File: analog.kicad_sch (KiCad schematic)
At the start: 21 parts, among them U10 OPA310xDBV, U11 MCP1501-30xSN, U12 MCP3561R-E/ST, U13 AD5761RBRUZ-RL7

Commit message: Fix Pranav review suggestions
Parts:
- D5: symbol Device:D_Photo -> Sensor_Optical:S5971
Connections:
- net GNDA: now also D5.2 (C), D5.3 (A); no longer D5.1 (K)
- net at C16.2, R6.1, U10.4 (-): now also D5.1 (K); no longer D5.2 (A)
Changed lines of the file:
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@@
+	)
+	(junction
+		(at 44.45 116.84)
+		(diameter 0)
+		(color 0 0 0 0)
 	)
 	(junction
@@
 	(wire
 		(pts
-			(xy 44.45 110.49) (xy 44.45 107.95)
-		)
-		(stroke
-			(width 0)
-			(type default)
-		)
-	)
-	(wire
-		(pts
 			(xy 144.78 118.11) (xy 144.78 116.84)
 		)
@@
 	(wire
 		(pts
+			(xy 36.83 107.95) (xy 36.83 116.84)
+		)
+		(stroke
+			(width 0)
+			(type default)
+		)
+	)
+	(wire
+		(pts
 			(xy 129.54 39.37) (xy 129.54 35.56)
 		)
@@
 	(wire
 		(pts
+			(xy 44.45 115.57) (xy 44.45 116.84)
+		)
+		(stroke
+			(width 0)
+			(type default)
+		)
+	)
+	(wire
+		(pts
 			(xy 227.33 82.55) (xy 233.68 82.55)
 		)
@@
 	(wire
 		(pts
+			(xy 44.45 116.84) (xy 44.45 118.11)
+		)
+		(stroke
+			(width 0)
+			(type default)
+		)
+	)
+	(wire
+		(pts
 			(xy 29.21 95.25) (xy 29.21 91.44)
 		)
@@
 		(pts
 			(xy 86.36 95.25) (xy 86.36 93.98)
+		)
+		(stroke
+			(width 0)
+			(type default)
+		)
+	)
+	(wire
+		(pts
+			(xy 36.83 116.84) (xy 44.45 116.84)
 		)
 		(stroke
@@
 	)
 	(symbol
-		(lib_id "Device:D_Photo")
-		(at 44.45 102.87 90)
+		(lib_id "Sensor_Optical:S5971")
+		(at 44.45 107.95 270)
 		(unit 1)
 		(exclude_from_sim no)
@@
 		(fields_autoplaced yes)
 		(property "Reference" "D5"
-			(at 46.99 102.5524 90)
-			(effects
-				(font
-					(size 1.27 1.27)
-				)
-				(justify right)
+			(at 49.53 106.6799 90)
+			(effects
+				(font
+					(size 1.27 1.27)
+				)
+				(justify left)
 			)
 		)
 		(property "Value" "D_Photo"
-			(at 46.99 105.0924 90)
-			(effects
-				(font
-					(size 1.27 1.27)
-				)
-				(justify right)
+			(at 49.53 109.2199 90)
+			(effects
+				(font
+					(size 1.27 1.27)
+				)
+				(justify left)
 			)
 		)
 		(property "Footprint" "Package_TO_SOT_THT:TO-5-3"
-			(at 44.45 104.14 0)
-			(effects
-				(font
-					(size 1.27 1.27)
-				)
-				(hide yes)
-			)
-		)
-		(property "Datasheet" "~"
-			(at 44.45 104.14 0)
-			(effects
-				(font
-					(size 1.27 1.27)
-				)
-				(hide yes)
-			)
-		)
-		(property "Description" "Photodiode"
-			(at 44.45 102.87 0)
+			(at 53.34 107.95 0)
+			(effects
+				(font
+					(size 1.27 1.27)
+				)
+				(hide yes)
+			)
+		)
+		(property "Datasheet" "https://www.hamamatsu.com/resources/pdf/ssd/s5971_etc_kpin1025e.pdf"
+			(at 44.45 107.95 0)
+			(effects
+				(font
+					(size 1.27 1.27)
+				)
+				(hide yes)
+			)
+		)
+		(property "Description" "Si PIN Photodiode, 0.1 GHz, TO-18-3"
+			(at 44.45 107.95 0)
 			(effects
 				(font
@@
 		)
 		(pin "1"
+		)
+		(pin "3"
 		)
 		(instances
@@
 	(symbol
 		(lib_id "power:GNDA")
-		(at 44.45 110.49 0)
+		(at 44.45 118.11 0)
 		(unit 1)
 		(exclude_from_sim no)
@@
 		(fields_autoplaced yes)
 		(property "Reference" "#PWR041"
-			(at 44.45 116.84 0)
+			(at 44.45 124.46 0)
 			(effects
 				(font
@@
 		)
 		(property "Value" "GNDA"
-			(at 44.45 115.57 0)
+			(at 44.45 123.19 0)
 			(effects
 				(font
@@
 		)
 		(property "Footprint" ""
-			(at 44.45 110.49 0)
+			(at 44.45 118.11 0)
 			(effects
 				(font
@@
 		)
 		(property "Datasheet" ""
-			(at 44.45 110.49 0)
+			(at 44.45 118.11 0)
 			(effects
 				(font
@@
 		)
 		(property "Description" "Power symbol creates a global label with name \"GNDA\" , analog ground"
-			(at 44.45 110.49 0)
-			(effects
-				(font
+			(at 44.45 118.11 0)
+			(effects
+				(font

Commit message: Fix review suggestions from non-fpga board
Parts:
- added C44: 10uF, Capacitor_SMD:C_0805_2012Metric_Pad1.18x1.45mm_HandSolder, symbol Device:C
- added R15: 10kR, Resistor_SMD:R_0805_2012Metric_Pad1.20x1.40mm_HandSolder, symbol Device:R_US
- added U16: OPA310xDBV, Package_TO_SOT_SMD:SOT-23-5, symbol Amplifier_Operational:OPA310xDBV
- C27: footprint Capacitor_SMD:C_0805_2012Metric_Pad1.18x1.45mm_HandSolder -> Capacitor_SMD:C_1210_3225Metric_Pad1.33x2.70mm_HandSolder
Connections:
- net +2V5: now also U13.4 (VREFIN/VREFOUT)
- net +3.3VA: now also U16.5 (V+)
- net GND: now also C26.2
- net GNDA: now also C44.2, U16.2 (V-)
- net at U11.7 (OUT), U11.8 (FB): now also R15.1; no longer U12.4 (REFIN+/OUT)
- net DAC_RST: now reaches U13.3 (*RESET)
- net SS0_an renamed ~{SS0_an}
- net SS1_an renamed ~{SS1_an}
- new net: C44.1, R15.2, U16.3 (+)
- new net: U12.4 (REFIN+/OUT), U16.1, U16.4 (-)
- no-connect marks 4 -> 3
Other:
- moved on the sheet: C14, C15, C16, C19, C23, C26, C27, D5, R4, R5, R6, U10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

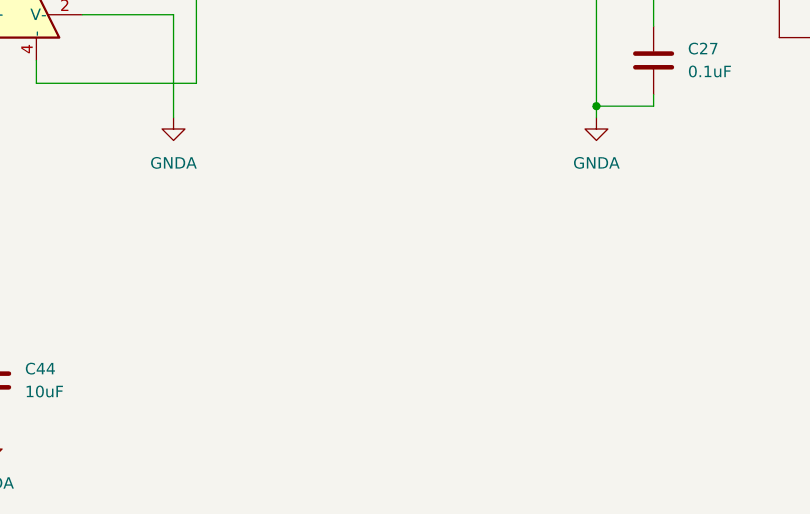
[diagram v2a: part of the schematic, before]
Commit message: Fix diode
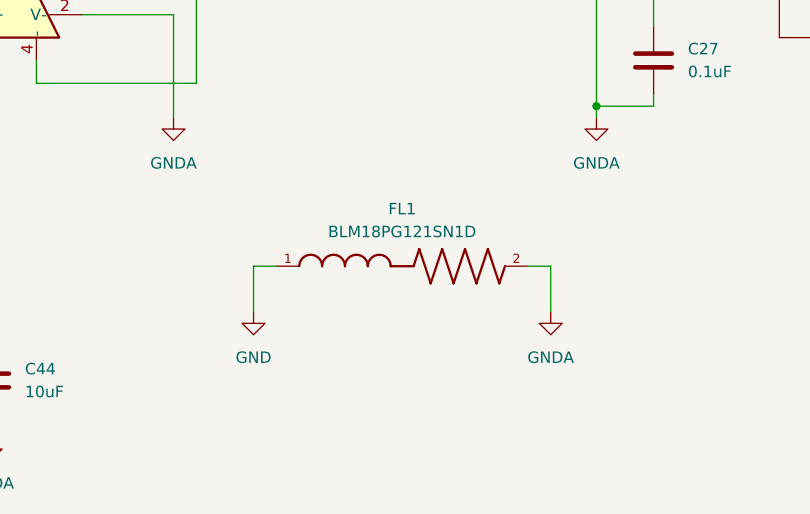
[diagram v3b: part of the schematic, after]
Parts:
- added FL1: BLM18PG121SN1D, fer:BEADC1608X95N, symbol fer:BLM18PG121SN1D
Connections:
- net GND: now also FL1.1
- net GNDA: now also FL1.2
